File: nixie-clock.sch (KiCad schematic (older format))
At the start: 1 part

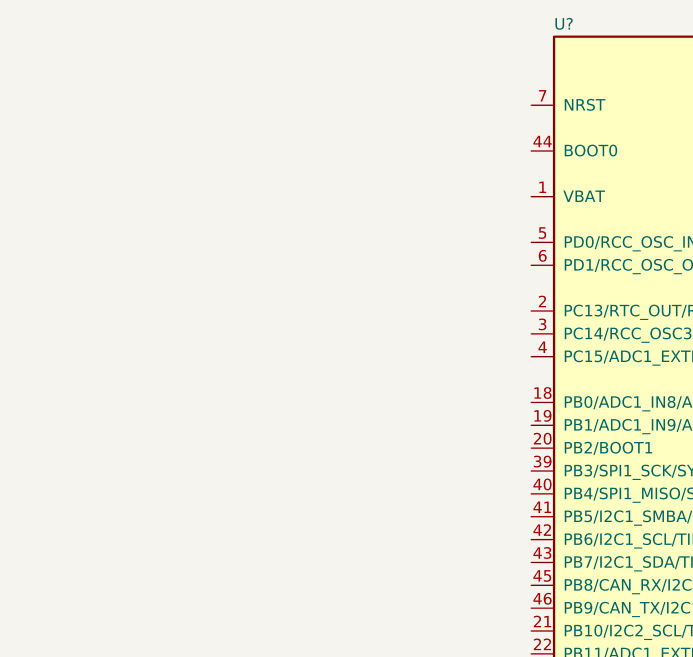
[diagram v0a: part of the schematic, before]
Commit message: Dodanie oscylatorow 8MHz i 32kHz
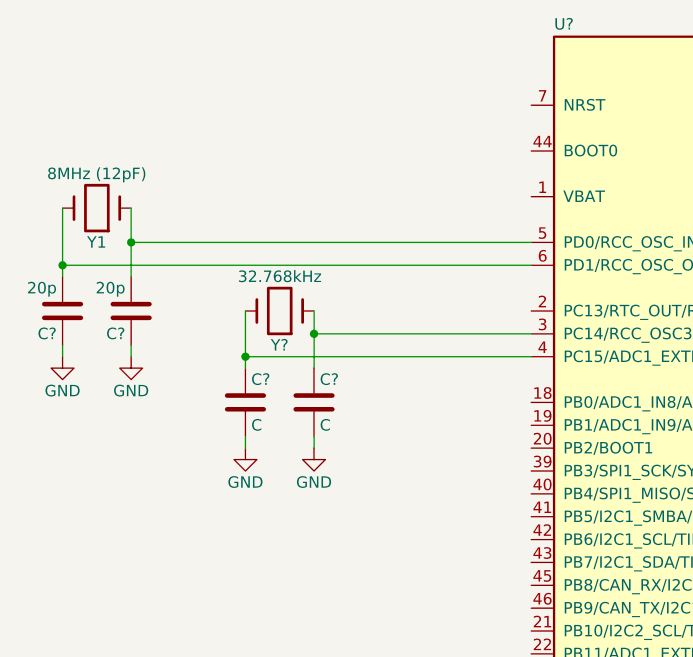
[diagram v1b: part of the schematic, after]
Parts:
- added C? (x2): 20p, symbol C
- added C? (x2): C, symbol C
- added Y1: 8MHz (12pF), symbol Crystal
- added Y?: 32.768kHz, symbol Crystal
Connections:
- net at U?.3 (PC14/RCC_OSC32_IN): now also C?.1, Y?.1
- net at U?.4 (PC15/ADC1_EXTI15/ADC2_EXTI15/RCC_OSC32_OUT): now also C?.1, Y?.2
- net at U?.5 (PD0/RCC_OSC_IN): now also C?.2, Y1.1
- net at U?.6 (PD1/RCC_OSC_OUT): now also C?.2, Y1.2
- new net GND: C?.1, C?.1, C?.2, C?.2
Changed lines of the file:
@@
 LIBS:valves
 LIBS:stm32
+LIBS:nixie-clock-cache
 EELAYER 25 0
 EELAYER END
@@
 	1    0    0    -1
 $EndComp
+$Comp
+L Crystal Y1
+U 1 1 5809E4B2
+P 1200 2900
+F 0 "Y1" H 1200 3050 50  0000 C CNN
+F 1 "8MHz (12pF)" H 1200 2750 50  0000 C CNN
+F 2 "" H 1200 2900 50  0000 C CNN
+F 3 "" H 1200 2900 50  0000 C CNN
+	1    1200 2900
+	-1   0    0    1
+$EndComp
+Wire Wire Line
+	3100 3050 1350 3050
+Wire Wire Line
+	1350 2900 1350 3050
+Wire Wire Line
+	1350 3050 1350 3200
+Wire Wire Line
+	3100 3150 1050 3150
+Wire Wire Line
+	1050 2900 1050 3150
+Wire Wire Line
+	1050 3150 1050 3200
+$Comp
+L C C?
+U 1 1 5809E60B
+P 1050 3350
+F 0 "C?" H 1075 3450 50  0000 L CNN
+F 1 "20p" H 1075 3250 50  0000 L CNN
+F 2 "" H 1088 3200 50  0000 C CNN
+F 3 "" H 1050 3350 50  0000 C CNN
+	1    1050 3350
+	-1   0    0    1
+$EndComp
+$Comp
+L C C?
+U 1 1 5809E7D7
+P 1350 3350
+F 0 "C?" H 1375 3450 50  0000 L CNN
+F 1 "20p" H 1375 3250 50  0000 L CNN
+F 2 "" H 1388 3200 50  0000 C CNN
+F 3 "" H 1350 3350 50  0000 C CNN
+	1    1350 3350
+	-1   0    0    1
+$EndComp
+Connection ~ 1050 3150
+Connection ~ 1350 3050
+$Comp
+L GND #PWR?
+U 1 1 5809E87F
+P 1050 3550
+F 0 "#PWR?" H 1050 3300 50  0001 C CNN
+F 1 "GND" H 1050 3400 50  0000 C CNN
+F 2 "" H 1050 3550 50  0000 C CNN
+F 3 "" H 1050 3550 50  0000 C CNN
+	1    1050 3550
+	1    0    0    -1
+$EndComp
+$Comp
+L GND #PWR?
+U 1 1 5809E959
+P 1350 3550
+F 0 "#PWR?" H 1350 3300 50  0001 C CNN
+F 1 "GND" H 1350 3400 50  0000 C CNN
+F 2 "" H 1350 3550 50  0000 C CNN
+F 3 "" H 1350 3550 50  0000 C CNN
+	1    1350 3550
+	1    0    0    -1
+$EndComp
+Wire Wire Line
+	1050 3500 1050 3550
+Wire Wire Line
+	1350 3500 1350 3550
+$Comp
+L Crystal Y?
+U 1 1 5809F07A
+P 2000 3350
+F 0 "Y?" H 2000 3500 50  0000 C CNN
+F 1 "32.768kHz" H 2000 3200 50  0000 C CNN
+F 2 "" H 2000 3350 50  0000 C CNN
+F 3 "" H 2000 3350 50  0000 C CNN
+F 4 "LFXTAL002996BULK" H 2000 3350 60  0001 C CNN "Oznaczenie"
+	1    2000 3350
+	-1   0    0    1
+$EndComp
+Wire Wire Line
+	2150 3350 2150 3450
+Wire Wire Line
+	2150 3450 2150 3600
+Wire Wire Line
+	2150 3450 3100 3450
+Wire Wire Line
+	1850 3350 1850 3550
+Wire Wire Line
+	1850 3550 1850 3600
+Wire Wire Line
+	1850 3550 3100 3550
+$Comp
+L C C?
+U 1 1 5809F25A
+P 1850 3750
+F 0 "C?" H 1875 3850 50  0000 L CNN
+F 1 "C" H 1875 3650 50  0000 L CNN
+F 2 "" H 1888 3600 50  0000 C CNN
+F 3 "" H 1850 3750 50  0000 C CNN
+	1    1850 3750
+	1    0    0    -1
+$EndComp
+$Comp
+L C C?
+U 1 1 5809F3ED
+P 2150 3750
+F 0 "C?" H 2175 3850 50  0000 L CNN
+F 1 "C" H 2175 3650 50  0000 L CNN
+F 2 "" H 2188 3600 50  0000 C CNN
+F 3 "" H 2150 3750 50  0000 C CNN
+	1    2150 3750
+	1    0    0    -1
+$EndComp
+$Comp
+L GND #PWR?
+U 1 1 5809F415
+P 1850 3950
+F 0 "#PWR?" H 1850 3700 50  0001 C CNN
+F 1 "GND" H 1850 3800 50  0000 C CNN
+F 2 "" H 1850 3950 50  0000 C CNN
+F 3 "" H 1850 3950 50  0000 C CNN
+	1    1850 3950
+	1    0    0    -1
+$EndComp
+$Comp
+L GND #PWR?
+U 1 1 5809F43C
+P 2150 3950
+F 0 "#PWR?" H 2150 3700 50  0001 C CNN
+F 1 "GND" H 2150 3800 50  0000 C CNN
+F 2 "" H 2150 3950 50  0000 C CNN
+F 3 "" H 2150 3950 50  0000 C CNN
+	1    2150 3950
+	1    0    0    -1
+$EndComp
+Connection ~ 1850 3550
+Connection ~ 2150 3450
+Wire Wire Line
+	1850 3900 1850 3950
+Wire Wire Line
+	2150 3900 2150 3950
 $EndSCHEMATC

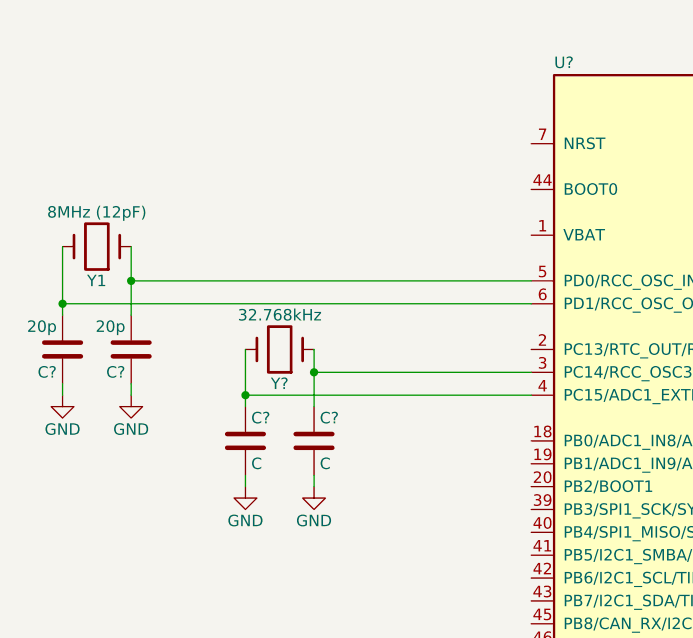
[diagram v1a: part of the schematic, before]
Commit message: Usuniecie oscylatora 8MHz; zasilanie bateryjne
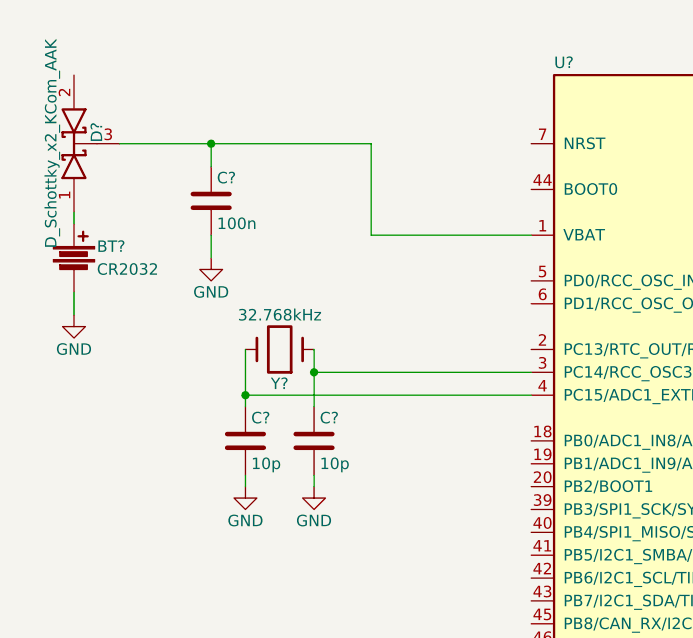
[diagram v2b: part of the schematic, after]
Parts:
- removed C? (x2): 20p, symbol C
- removed Y1: 8MHz (12pF), symbol Crystal
- added BT?: CR2032, symbol Battery
- added C?: 100n, symbol C
- added D?: D_Schottky_x2_KCom_AAK, symbol D_Schottky_x2_KCom_AAK
- C? (x2): value C -> 10p
- Y?: Oznaczenie LFXTAL002996BULK -> (none); Part no. (none) -> LFXTAL002996BULK
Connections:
- net GND: now also BT?.2, C?.2
- net at U?.1 (VBAT): now also C?.1, D?.3 (K)
- new net: BT?.1, D?.1 (A)
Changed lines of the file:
@@
 $EndComp
-$Comp
-L Crystal Y1
-U 1 1 5809E4B2
-P 1200 2900
-F 0 "Y1" H 1200 3050 50  0000 C CNN
-F 1 "8MHz (12pF)" H 1200 2750 50  0000 C CNN
-F 2 "" H 1200 2900 50  0000 C CNN
-F 3 "" H 1200 2900 50  0000 C CNN
-	1    1200 2900
-	-1   0    0    1
-$EndComp
-Wire Wire Line
-	3100 3050 1350 3050
-Wire Wire Line
-	1350 2900 1350 3050
-Wire Wire Line
-	1350 3050 1350 3200
-Wire Wire Line
-	3100 3150 1050 3150
-Wire Wire Line
-	1050 2900 1050 3150
-Wire Wire Line
-	1050 3150 1050 3200
-$Comp
-L C C?
-U 1 1 5809E60B
-P 1050 3350
-F 0 "C?" H 1075 3450 50  0000 L CNN
-F 1 "20p" H 1075 3250 50  0000 L CNN
-F 2 "" H 1088 3200 50  0000 C CNN
-F 3 "" H 1050 3350 50  0000 C CNN
-	1    1050 3350
-	-1   0    0    1
-$EndComp
-$Comp
-L C C?
-U 1 1 5809E7D7
-P 1350 3350
-F 0 "C?" H 1375 3450 50  0000 L CNN
-F 1 "20p" H 1375 3250 50  0000 L CNN
-F 2 "" H 1388 3200 50  0000 C CNN
-F 3 "" H 1350 3350 50  0000 C CNN
-	1    1350 3350
-	-1   0    0    1
-$EndComp
-Connection ~ 1050 3150
-Connection ~ 1350 3050
-$Comp
-L GND #PWR?
-U 1 1 5809E87F
-P 1050 3550
-F 0 "#PWR?" H 1050 3300 50  0001 C CNN
-F 1 "GND" H 1050 3400 50  0000 C CNN
-F 2 "" H 1050 3550 50  0000 C CNN
-F 3 "" H 1050 3550 50  0000 C CNN
-	1    1050 3550
-	1    0    0    -1
-$EndComp
-$Comp
-L GND #PWR?
-U 1 1 5809E959
-P 1350 3550
-F 0 "#PWR?" H 1350 3300 50  0001 C CNN
-F 1 "GND" H 1350 3400 50  0000 C CNN
-F 2 "" H 1350 3550 50  0000 C CNN
-F 3 "" H 1350 3550 50  0000 C CNN
-	1    1350 3550
-	1    0    0    -1
-$EndComp
-Wire Wire Line
-	1050 3500 1050 3550
-Wire Wire Line
-	1350 3500 1350 3550
 $Comp
 L Crystal Y?
@@
 F 2 "" H 2000 3350 50  0000 C CNN
 F 3 "" H 2000 3350 50  0000 C CNN
-F 4 "LFXTAL002996BULK" H 2000 3350 60  0001 C CNN "Oznaczenie"
+F 4 "LFXTAL002996BULK" H 2000 3350 60  0001 C CNN "Part no."
 	1    2000 3350
 	-1   0    0    1
 $EndComp
 Wire Wire Line
-	2150 3350 2150 3450
-Wire Wire Line
-	2150 3450 2150 3600
+	2150 3350 2150 3600
 Wire Wire Line
 	2150 3450 3100 3450
 Wire Wire Line
-	1850 3350 1850 3550
-Wire Wire Line
-	1850 3550 1850 3600
+	1850 3350 1850 3600
 Wire Wire Line
 	1850 3550 3100 3550
@@
 P 1850 3750
 F 0 "C?" H 1875 3850 50  0000 L CNN
-F 1 "C" H 1875 3650 50  0000 L CNN
+F 1 "10p" H 1875 3650 50  0000 L CNN
 F 2 "" H 1888 3600 50  0000 C CNN
 F 3 "" H 1850 3750 50  0000 C CNN
@@
 P 2150 3750
 F 0 "C?" H 2175 3850 50  0000 L CNN
-F 1 "C" H 2175 3650 50  0000 L CNN
+F 1 "10p" H 2175 3650 50  0000 L CNN
 F 2 "" H 2188 3600 50  0000 C CNN
 F 3 "" H 2150 3750 50  0000 C CNN
@@
 Wire Wire Line
 	2150 3900 2150 3950
+$Comp
+L D_Schottky_x2_KCom_AAK D?
+U 1 1 580A07B6
+P 1100 2450
+F 0 "D?" H 1150 2350 50  0000 C CNN
+F 1 "D_Schottky_x2_KCom_AAK" H 1100 2550 50  0000 C CNN
+F 2 "" H 1100 2450 50  0000 C CNN
+F 3 "" H 1100 2450 50  0000 C CNN
+	1    1100 2450
+	0    -1   -1   0
+$EndComp
+Wire Wire Line
+	1300 2450 2400 2450
+Wire Wire Line
+	2400 2450 2400 2850
+Wire Wire Line
+	2400 2850 3100 2850
+Wire Wire Line
+	1700 2550 1700 2450
+Connection ~ 1700 2450
+$Comp
+L C C?
+U 1 1 580A0B7E
+P 1700 2700
+F 0 "C?" H 1725 2800 50  0000 L CNN
+F 1 "100n" H 1725 2600 50  0000 L CNN
+F 2 "" H 1738 2550 50  0000 C CNN
+F 3 "" H 1700 2700 50  0000 C CNN
+	1    1700 2700
+	1    0    0    -1
+$EndComp
+$Comp
+L GND #PWR?
+U 1 1 580A0C6B
+P 1700 2950
+F 0 "#PWR?" H 1700 2700 50  0001 C CNN
+F 1 "GND" H 1700 2800 50  0000 C CNN
+F 2 "" H 1700 2950 50  0000 C CNN
+F 3 "" H 1700 2950 50  0000 C CNN
+	1    1700 2950
+	1    0    0    -1
+$EndComp
+Wire Wire Line
+	1700 2950 1700 2850
+$Comp
+L Battery BT?
+U 1 1 580A0D26
+P 1100 2950
+F 0 "BT?" H 1200 3000 50  0000 L CNN
+F 1 "CR2032" H 1200 2900 50  0000 L CNN
+F 2 "" V 1100 2990 50  0000 C CNN
+F 3 "" V 1100 2990 50  0000 C CNN
+	1    1100 2950
+	1    0    0    -1
+$EndComp
+Wire Wire Line
+	1100 2800 1100 2750
+$Comp
+L GND #PWR?
+U 1 1 580A0DB8
+P 1100 3200
+F 0 "#PWR?" H 1100 2950 50  0001 C CNN
+F 1 "GND" H 1100 3050 50  0000 C CNN
+F 2 "" H 1100 3200 50  0000 C CNN
+F 3 "" H 1100 3200 50  0000 C CNN
+	1    1100 3200
+	1    0    0    -1
+$EndComp
+Wire Wire Line
+	1100 3100 1100 3200
 $EndSCHEMATC
